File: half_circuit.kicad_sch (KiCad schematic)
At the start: 20 parts, among them J11 Select, J13 Inh, J15 4046 Comp In, J17 4046 Out, J19 4040 Input, J21 4053 S3, J23 4053 C, J25 4053 C0 C1, J27 4040 Output, J29 4017 Fdbk, J33 4017 Pins, J5 Input, J7 4046 SigIn, J8 4046 Comp, Q1 2N3904, Q3 2N3904, SW1 4046 CompIn, SW3 4017 Feedback

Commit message: start smd refactoring
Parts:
- Q1, Q3: footprint Package_TO_SOT_THT:TO-92_Inline_Wide -> SOT-23; KiLib_Generator (none) -> package/gullwing
- R1, R6: footprint Resistor_THT:R_Axial_DIN0207_L6.3mm_D2.5mm_P10.16mm_Horizontal -> R_0805_2012Metric; KiLib_Generator (none) -> SMD_2terminal_chip_molded
- SW1: footprint Button_Switch_THT:SW_E-Switch_EG1271_SPDT -> SW_SPDT_CK_JS102011SAQN
- SW3: footprint Button_Switch_THT:SW_CK_JS202011CQN_DPDT_Straight -> SW_DPDT_CK_JS202011JCQN
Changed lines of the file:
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@@
 			)
 		)
-		(property "Footprint" "Button_Switch_THT:SW_E-Switch_EG1271_SPDT"
+		(property "Footprint" "SW_SPDT_CK_JS102011SAQN"
 			(at 109.22 52.07 0)
 			(hide yes)
@@
 			)
 		)
-		(property "Description" "Switch, single pole double throw"
+		(property "Description" ""
 			(at 109.22 52.07 0)
 			(hide yes)
@@
 			)
 		)
-		(property "Footprint" "Package_TO_SOT_THT:TO-92_Inline_Wide"
+		(property "Footprint" "SOT-23"
 			(at 129.54 90.805 0)
 			(hide yes)
@@
 			)
 		)
-		(property "Datasheet" "https://www.onsemi.com/pub/Collateral/2N3903-D.PDF"
+		(property "Datasheet" ""
 			(at 124.46 88.9 0)
 			(hide yes)
@@
 			)
 		)
-		(property "Description" "0.2A Ic, 40V Vce, Small Signal NPN Transistor, TO-92"
+		(property "Description" ""
+			(at 124.46 88.9 0)
+			(hide yes)
+			(show_name no)
+			(do_not_autoplace no)
+			(effects
+				(font
+					(size 1.27 1.27)
+				)
+			)
+		)
+		(property "KiLib_Generator" "package/gullwing"
 			(at 124.46 88.9 0)
 			(hide yes)
@@
 			)
 		)
-		(property "Footprint" "Package_TO_SOT_THT:TO-92_Inline_Wide"
+		(property "Footprint" "SOT-23"
 			(at 58.42 62.865 0)
 			(hide yes)
@@
 			)
 		)
-		(property "Datasheet" "https://www.onsemi.com/pub/Collateral/2N3903-D.PDF"
+		(property "Datasheet" ""
 			(at 53.34 60.96 0)
 			(hide yes)
@@
 			)
 		)
-		(property "Description" "0.2A Ic, 40V Vce, Small Signal NPN Transistor, TO-92"
+		(property "Description" ""
+			(at 53.34 60.96 0)
+			(hide yes)
+			(show_name no)
+			(do_not_autoplace no)
+			(effects
+				(font
+					(size 1.27 1.27)
+				)
+			)
+		)
+		(property "KiLib_Generator" "package/gullwing"
 			(at 53.34 60.96 0)
 			(hide yes)
@@
 			)
 		)
-		(property "Footprint" "Resistor_THT:R_Axial_DIN0207_L6.3mm_D2.5mm_P10.16mm_Horizontal"
+		(property "Footprint" "R_0805_2012Metric"
 			(at 55.88 68.58 0)
 			(hide yes)
@@
 			)
 		)
-		(property "Description" "Resistor, small symbol"
+		(property "Description" ""
+			(at 55.88 68.58 0)
+			(hide yes)
+			(show_name no)
+			(do_not_autoplace no)
+			(effects
+				(font
+					(size 1.27 1.27)
+				)
+			)
+		)
+		(property "KiLib_Generator" "SMD_2terminal_chip_molded"
 			(at 55.88 68.58 0)
 			(hide yes)
@@
 			)
 		)
-		(property "Footprint" "Resistor_THT:R_Axial_DIN0207_L6.3mm_D2.5mm_P10.16mm_Horizontal"
+		(property "Footprint" "R_0805_2012Metric"
 			(at 127 96.52 0)
 			(hide yes)
@@
 			)
 		)
-		(property "Description" "Resistor, small symbol"
+		(property "Description" ""
+			(at 127 96.52 0)
+			(hide yes)
+			(show_name no)
+			(do_not_autoplace no)
+			(effects
+				(font
+					(size 1.27 1.27)
+				)
+			)
+		)
+		(property "KiLib_Generator" "SMD_2terminal_chip_molded"
 			(at 127 96.52 0)
 			(hide yes)
@@
 			)
 		)
-		(property "Footprint" "Button_Switch_THT:SW_CK_JS202011CQN_DPDT_Straight"
+		(property "Footprint" "SW_DPDT_CK_JS202011JCQN"
 			(at 220.98 41.91 0)
 			(hide yes)
@@
 			)
 		)
-		(property "Description" "Switch, dual pole double throw, separate symbols"
+		(property "Description" ""
 			(at 220.98 41.91 0)
 			(hide yes)
@@
 			)
 		)
+		(instances
+			(project "kleingorium"
+				(path "/01c1f2c1-4d06-4880-847a-9ab55552e3fd/ad1f1d92-237d-4bc3-883c-2ce266dd223f/e00ebc01-440e-4477-8d51-aed2c51c95ea"
+					(page "8")
+				)
+				(path "/01c1f2c1-4d06-4880-847a-9ab55552e3fd/ad1f1d92-237d-4bc3-883c-2ce266dd223f/4b203833-f0af-4e88-a9fb-191df5175df3"
+					(page "19")
+				)
+			)
+		)
 	)
 	(sheet
@@
 			)
 		)
+		(instances
+			(project "kleingorium"
+				(path "/01c1f2c1-4d06-4880-847a-9ab55552e3fd/ad1f1d92-237d-4bc3-883c-2ce266dd223f/e00ebc01-440e-4477-8d51-aed2c51c95ea"
+					(page "3")
+				)
+				(path "/01c1f2c1-4d06-4880-847a-9ab55552e3fd/ad1f1d92-237d-4bc3-883c-2ce266dd223f/4b203833-f0af-4e88-a9fb-191df5175df3"
+					(page "15")
+				)
+			)
+		)
 	)
 	(sheet
@@
 			)
 		)
+		(instances
+			(project "kleingorium"
+				(path "/01c1f2c1-4d06-4880-847a-9ab55552e3fd/ad1f1d92-237d-4bc3-883c-2ce266dd223f/e00ebc01-440e-4477-8d51-aed2c51c95ea"
+					(page "4")
+				)
+				(path "/01c1f2c1-4d06-4880-847a-9ab55552e3fd/ad1f1d92-237d-4bc3-883c-2ce266dd223f/4b203833-f0af-4e88-a9fb-191df5175df3"
+					(page "16")
+				)
+			)
+		)
 	)
 	(sheet
@@
 			)
 		)
+		(instances
+			(project "kleingorium"
+				(path "/01c1f2c1-4d06-4880-847a-9ab55552e3fd/ad1f1d92-237d-4bc3-883c-2ce266dd223f/e00ebc01-440e-4477-8d51-aed2c51c95ea"
+					(page "7")
+				)
+				(path "/01c1f2c1-4d06-4880-847a-9ab55552e3fd/ad1f1d92-237d-4bc3-883c-2ce266dd223f/4b203833-f0af-4e88-a9fb-191df5175df3"
+					(page "17")
+				)
+			)
+		)

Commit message: back to kicad 10.0
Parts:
- SW1: footprint SW_SPDT_CK_JS102011SAQN -> Button_Switch_THT:SW_Slide_SPDT_Straight_CK_OS102011MS2Q
- SW3: footprint SW_DPDT_CK_JS202011JCQN -> Button_Switch_THT:SW_Slide_SPDT_Straight_CK_OS102011MS2Q
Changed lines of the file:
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@@
 (kicad_sch
-	(version 20260826)
+	(version 20260306)
 	(generator "eeschema")
-	(generator_version "10.99")
+	(generator_version "10.0")
 	(paper "A4")
 	(junction
@@
 			)
 		)
-		(property "Footprint" "SW_SPDT_CK_JS102011SAQN"
+		(property "Footprint" "Button_Switch_THT:SW_Slide_SPDT_Straight_CK_OS102011MS2Q"
 			(at 109.22 52.07 0)
 			(hide yes)
@@
 			)
 		)
-		(property "Footprint" "SW_DPDT_CK_JS202011JCQN"
+		(property "Footprint" "Button_Switch_THT:SW_Slide_SPDT_Straight_CK_OS102011MS2Q"
 			(at 220.98 41.91 0)
 			(hide yes)

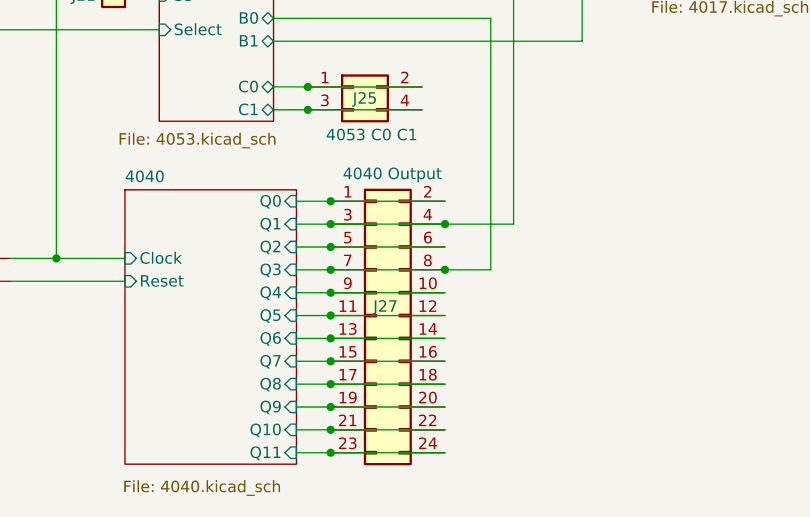
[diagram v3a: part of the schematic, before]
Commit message: drop 4040 outputs, rerouting
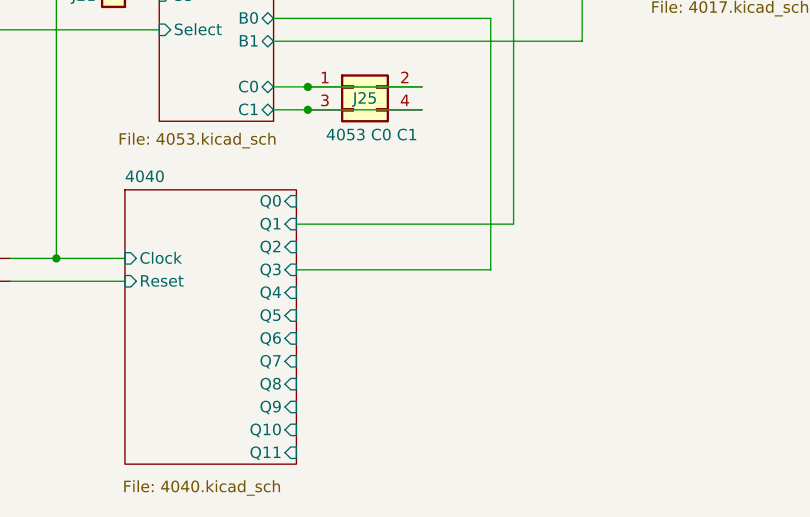
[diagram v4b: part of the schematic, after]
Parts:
- removed J27: 4040 Output, Connector_PinHeader_2.54mm:PinHeader_2x12_P2.54mm_Vertical, symbol Connector_Generic:Conn_02x12_Odd_Even
